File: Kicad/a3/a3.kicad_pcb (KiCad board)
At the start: 2 copper layers, 190 x 100 mm, 123 parts, among them J1 Barrel Jack, J2 IDC 34, J3 Conn_02x03_Odd_Even, J4 VGA, J5 AudioJack4, J6 DE9_Plug, J7 DE9_Plug, SW1 SW_Push, SW10 Y, SW11 I, SW12 P, SW13 A, SW14 D, SW15 G, SW16 J, SW17 L, SW18 S, SW19 F, SW2 SW_SPDT, SW20 H, SW21 K, SW22 ENT, SW23 SHIFT, SW24 X, SW25 V, SW26 N, SW27 SPACE, SW28 Z, SW29 C, SW3 Q, SW30 B, SW31 M, SW32 ALT, SW4 E, SW5 T, SW6 U, SW7 O, SW8 W, SW9 R, U1 74HC590A, U10 74HC32, U11 74HC4520, U12 74HC174, U13 MCP100H, U2 74HC590A, U3 SST39SF0x0, U4 62256, U5 W65C02SxP, U6 74HCT540, U7 74HC166, U8 74HCT04, U9 74HC10, Y1 16Mhz

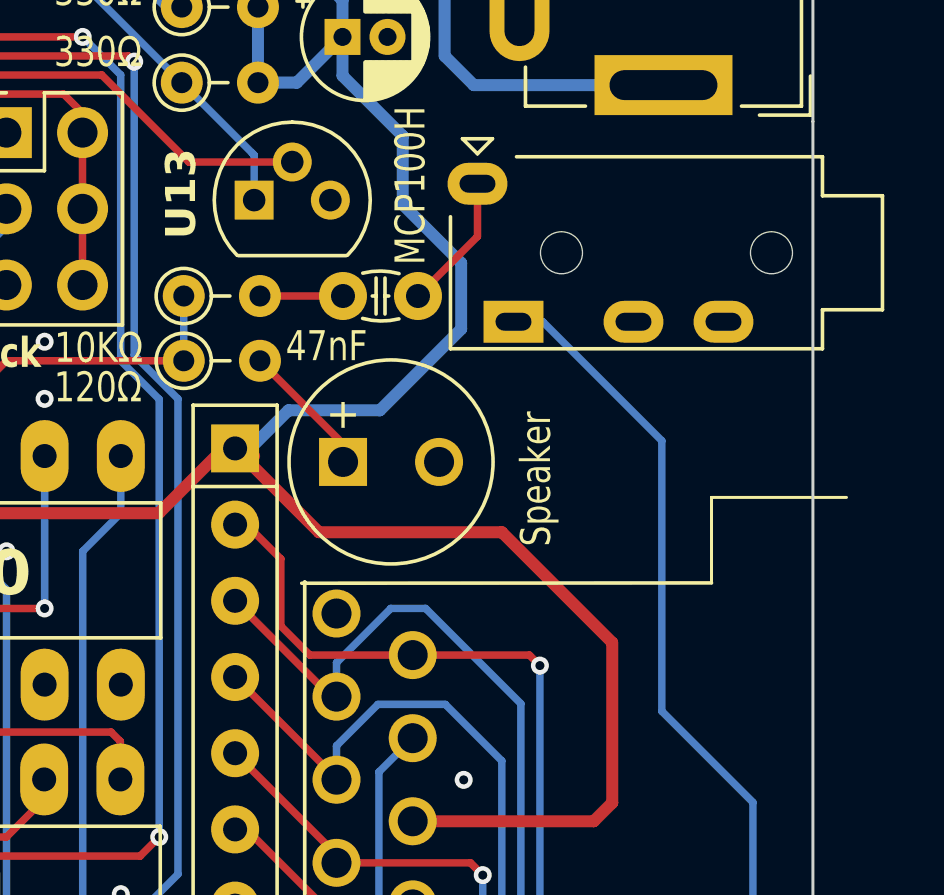
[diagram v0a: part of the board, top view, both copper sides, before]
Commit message: Add TTL/MIC level jumper to trs jack
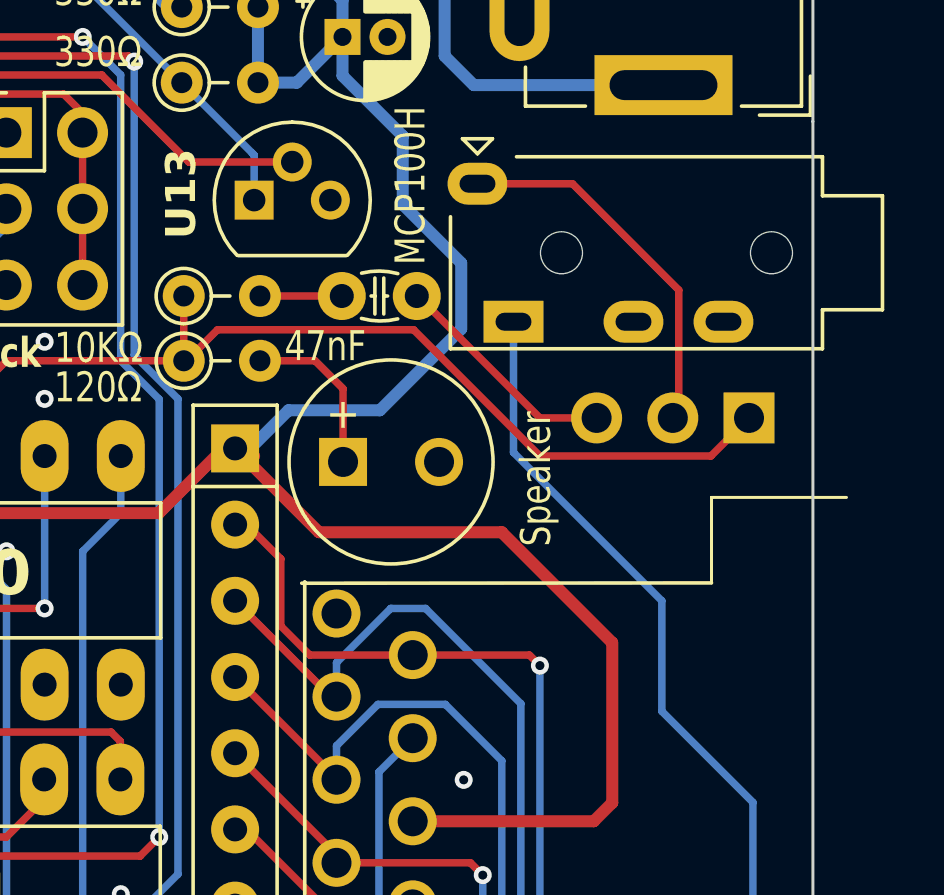
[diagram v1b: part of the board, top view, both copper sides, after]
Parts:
- added J8: Conn_01x03, Connector_PinHeader_2.54mm:PinHeader_1x03_P2.54mm_Vertical, B.Cu at (222.9, 55.9)
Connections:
- C10 pad 1: /DataOut -> Net-(J8-Pin_3)
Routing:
- net /BEEP: track 117.9 -> 139.4 mm
- net /DataOut: track 5.29 -> 13.3 mm
- net Net-(J8-Pin_3): track 0.00 -> 7.64 mm
- net Net-(C10-Pad2): track 2.24 -> 3.25 mm
- net /DataIn: track 167.1 -> 166.5 mm
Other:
- board text added: "MIC"
- board text added: "TTL"
